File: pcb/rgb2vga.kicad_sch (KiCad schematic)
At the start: 43 parts, among them J1 GPIO_0, J2 RGB_IN, J3 COCO3_RGB_IN, J4 C_VIDEO_IN, J5 GPIO_1, J6 VGA_OUT, J7 Conn_01x03_Male, SW1 SW_DIP_x10, SW2 SW_DP3T, U1 LM1881

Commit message: fiducials, pics
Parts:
- added JP1: lowpass, 000_LOCAL:JP_0805, symbol 000_LOCAL:SolderJumper_2_Bridged
- R29: footprint 000_LOCAL:R_0805_SJC -> 000_LOCAL:R_0805
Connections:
- net RGB_CS: now also JP1.1 (A)
- net at C1.1, C4.1, R29.2: now also JP1.2 (B)
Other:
- note added: "optional 500kHz low pass cut JP1"
- note removed: "optional 500kHz low pass"
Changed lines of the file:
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@@
 	(title_block
 		(title "DE0-NANO RGB2VGA")
-		(date "2024-01-07")
-		(rev "008")
+		(date "2024-07-26")
+		(rev "009")
 		(company "Brian K. White - b.kenyon.w@gmail.com")
 		(comment 1 "Original Design by Luis Antoniosi 2014")
@@
 	)
 	(junction
+		(at 180.34 134.62)
+		(diameter 0)
+		(color 0 0 0 0)
+	)
+	(junction
 		(at 127 81.28)
 		(diameter 0)
@@
 	)
 	(junction
+		(at 172.72 127)
+		(diameter 0)
+		(color 0 0 0 0)
+	)
+	(junction
 		(at 69.85 38.1)
 		(diameter 0)
@@
 	(wire
 		(pts
-			(xy 172.72 134.62) (xy 187.96 134.62)
+			(xy 172.72 134.62) (xy 180.34 134.62)
 		)
 		(stroke
@@
 	(wire
 		(pts
+			(xy 180.34 134.62) (xy 187.96 134.62)
+		)
+		(stroke
+			(width 0)
+			(type default)
+		)
+	)
+	(wire
+		(pts
 			(xy 203.2 66.04) (xy 190.5 66.04)
 		)
@@
 	(wire
 		(pts
+			(xy 172.72 127) (xy 180.34 127)
+		)
+		(stroke
+			(width 0)
+			(type default)
+		)
+	)
+	(wire
+		(pts
 			(xy 44.45 157.48) (xy 44.45 165.1)
 		)
@@
 		)
 	)
-	(text "optional\n500kHz\nlow pass"
+	(text "optional\n500kHz\nlow pass\ncut JP1"
 		(exclude_from_sim no)
 		(at 167.64 124.46 0)
@@
 	)
 	(symbol
+		(lib_id "000_LOCAL:SolderJumper_2_Bridged")
+		(at 180.34 130.81 270)
+		(unit 1)
+		(exclude_from_sim no)
+		(in_bom yes)
+		(on_board yes)
+		(dnp no)
+		(property "Reference" "JP1"
+			(at 180.848 126.238 90)
+			(effects
+				(font
+					(size 1.27 1.27)
+				)
+				(justify left)
+			)
+		)
+		(property "Value" "lowpass"
+			(at 180.594 124.206 90)
+			(effects
+				(font
+					(size 1.27 1.27)
+				)
+			)
+		)
+		(property "Footprint" "000_LOCAL:JP_0805"
+			(at 180.34 130.81 0)
+			(effects
+				(font
+					(size 1.27 1.27)
+				)
+				(hide yes)
+			)
+		)
+		(property "Datasheet" "~"
+			(at 180.34 130.81 0)
+			(effects
+				(font
+					(size 1.27 1.27)
+				)
+				(hide yes)
+			)
+		)
+		(property "Description" "Solder Jumper, 2-pole, closed/bridged"
+			(at 180.34 130.81 0)
+			(effects
+				(font
+					(size 1.27 1.27)
+				)
+				(hide yes)
+			)
+		)
+		(pin "1"
+		)
+		(pin "2"
+		)
+		(instances
+			(project ""
+				(path "/dc38b7f3-94d8-459d-903b-54a6ae2cb037"
+					(reference "JP1")
+					(unit 1)
+				)
+			)
+		)
+	)
+	(symbol
 		(lib_id "000_LOCAL:GND")
 		(at 133.35 127 0)
@@
 			)
 		)
-		(property "Footprint" "000_LOCAL:R_0805_SJC"
+		(property "Footprint" "000_LOCAL:R_0805"
 			(at 172.72 130.81 0)
 			(effects

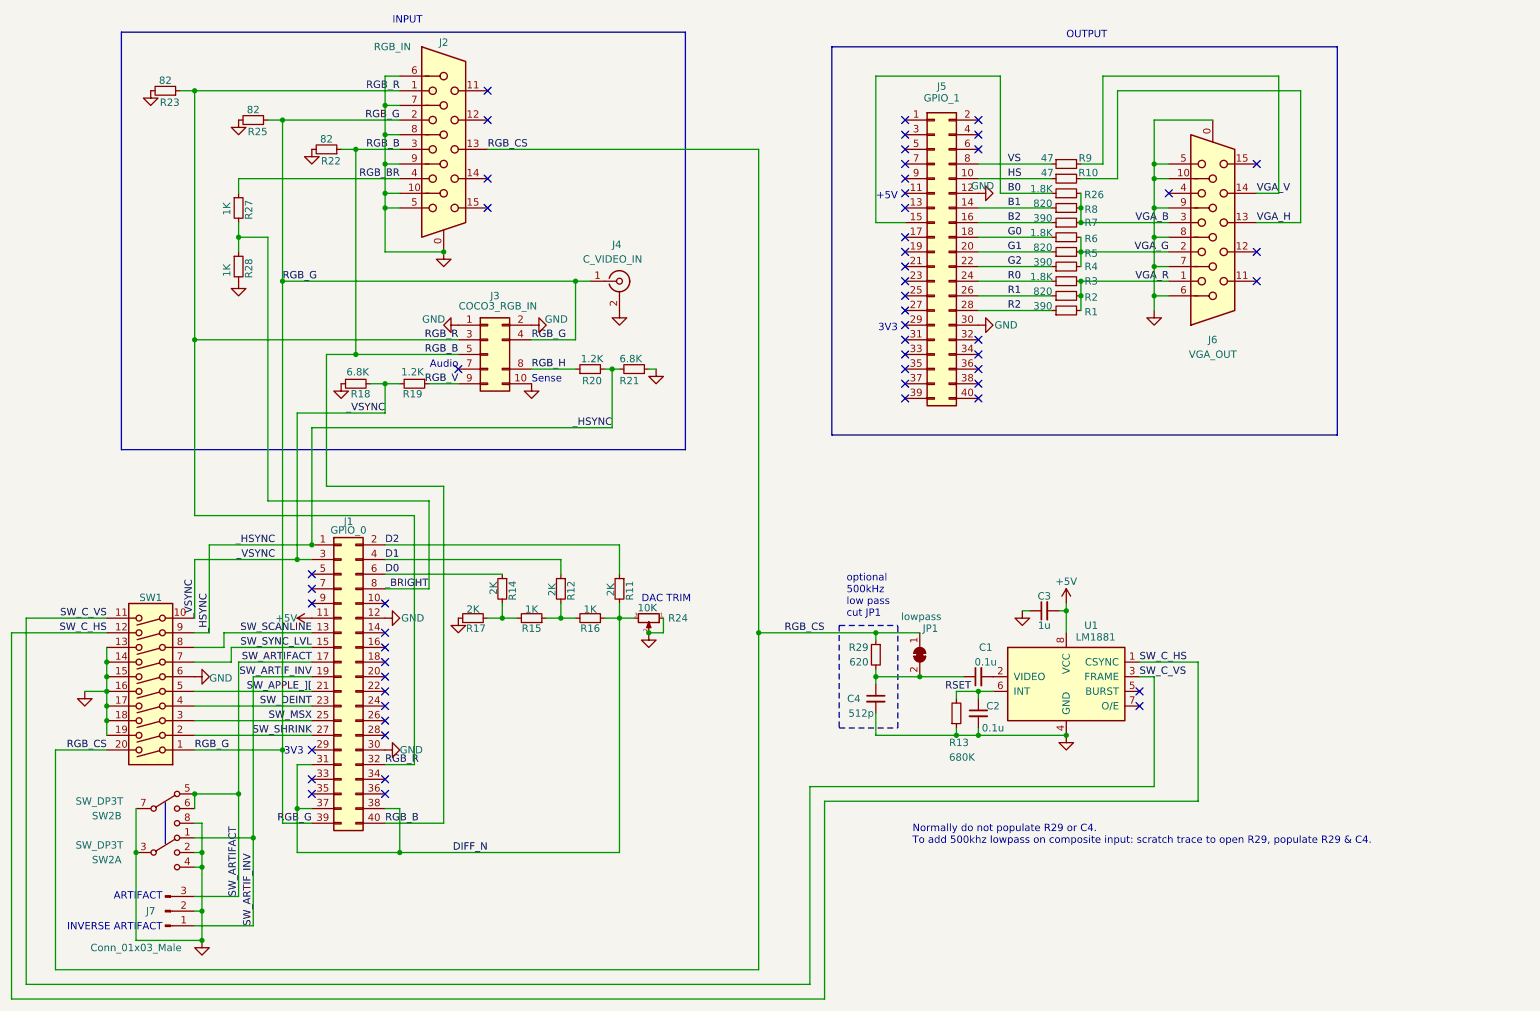
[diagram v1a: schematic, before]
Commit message: C4 510p, dnp fiducials, pnp export
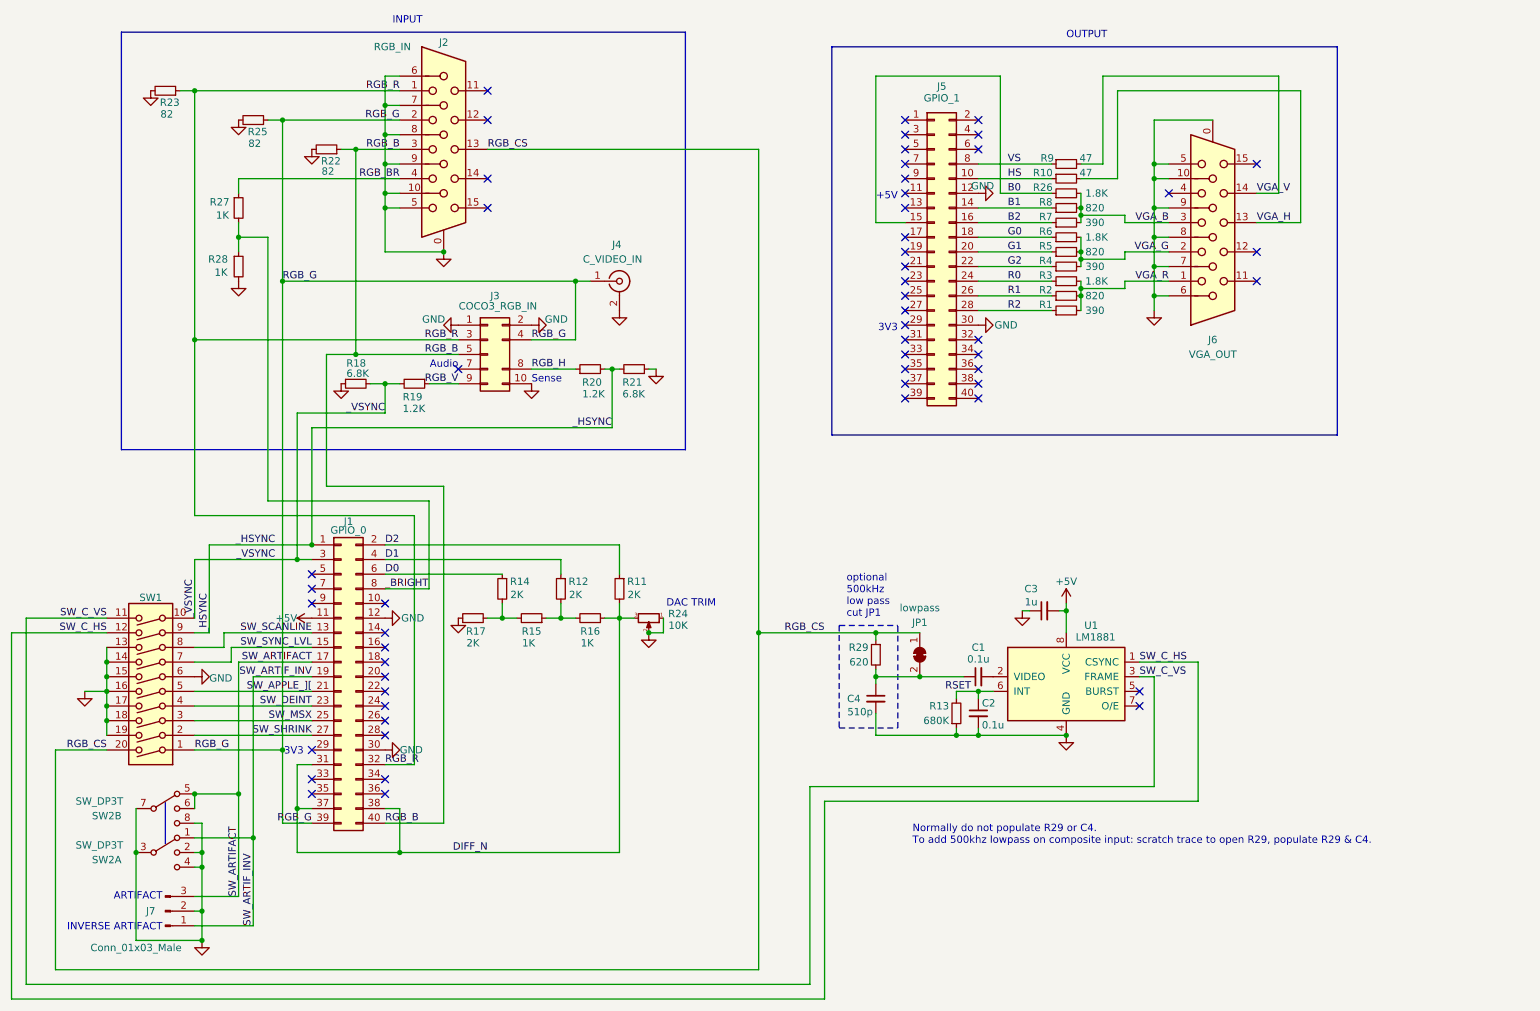
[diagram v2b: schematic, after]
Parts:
- C4: value 512p -> 510p

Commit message: export bom, centroid
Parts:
- C1, C2: MPN (none) -> KGM21NR71H104JT
- C3: MPN (none) -> CL21B105KAFNNNE
- C4: MPN (none) -> C0805C511F3HAC7800; now not fitted
- J1: value GPIO_0 -> PinSocket_02x20_P2.54mm_Vertical_tht; Label (none) -> GPIO_0; MPN (none) -> SFH11-PBPC-D20-ST-BK
- J2: value RGB_IN -> HD15F_horizontal_tht; Label (none) -> RGB_IN; MPN (none) -> HD15-SN-25
- J3: value COCO3_RGB_IN -> IDC-Header_2x05_P2.54mm_Horizontal_tht; Label (none) -> COCO3_RGB_IN; MPN (none) -> 302-R101
- J4: value C_VIDEO_IN -> RCA_horizontal_tht; Label (none) -> C_VIDEO_IN; MPN (none) -> RCJ-014
- J5: value GPIO_1 -> PinSocket_02x20_P2.54mm_Vertical_tht; Label (none) -> GPIO_1; MPN (none) -> SFH11-PBPC-D20-ST-BK
- J6: value VGA_OUT -> HD15F_horizontal_tht; Label (none) -> VGA_OUT; MPN (none) -> HD15-SN-25
- J7: MPN (none) -> PRPC003SBAN-M71RC
- JP1: now left out of the parts list
- R1, R4, R7: MPN (none) -> ERA-6AEB391V
- R10, R9: MPN (none) -> ERA-6AEB470V
- R11, R12, R14, R17: MPN (none) -> ERA-6AEB202V
- R13: MPN (none) -> ERA-6AEB684V
- R15, R16, R27, R28: MPN (none) -> ERA-6AEB102V
- R18, R21: MPN (none) -> ERA-6AEB682V
- R19, R20: MPN (none) -> ERA-6AEB122V
- R2, R5, R8: MPN (none) -> ERA-6AEB821V
- R22, R23, R25: MPN (none) -> ERA-6AEB820V
- R24: MPN (none) -> 3006P-1-103LF
- R26, R3, R6: MPN (none) -> ERA-6AEB182V
- R29: MPN (none) -> ERA-6AEB621V; now not fitted
- SW1: MPN (none) -> DS04-254-2-10BK-SMT
- SW2: MPN (none) -> CL-SB-23A-11T
- U1: MPN (none) -> LM1881MX/NOPB

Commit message: silkscreen & pics
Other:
- note added: "ADC TRIM"
- note removed: "DAC TRIM"
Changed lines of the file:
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@@
 	(title_block
 		(title "DE0-NANO RGB2VGA")
-		(date "2024-08-06")
-		(rev "010")
+		(date "2024-08-30")
+		(rev "018")
 		(company "Brian K. White - b.kenyon.w@gmail.com")
 		(comment 1 "Original Design by Luis Antoniosi 2014")
@@
 		)
 	)
-	(text "DAC TRIM"
+	(text "ADC TRIM"
 		(exclude_from_sim no)
 		(at 136.398 122.682 0)

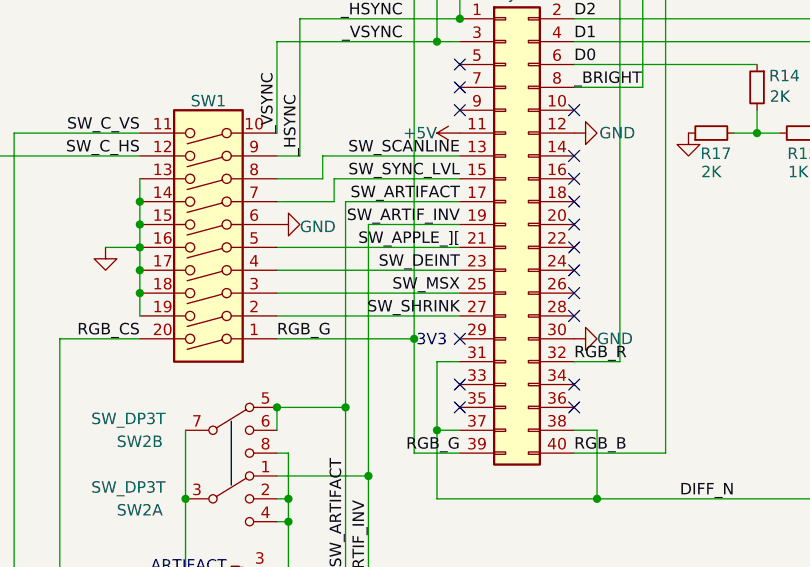
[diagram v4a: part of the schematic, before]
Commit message: rename msx switch to offset
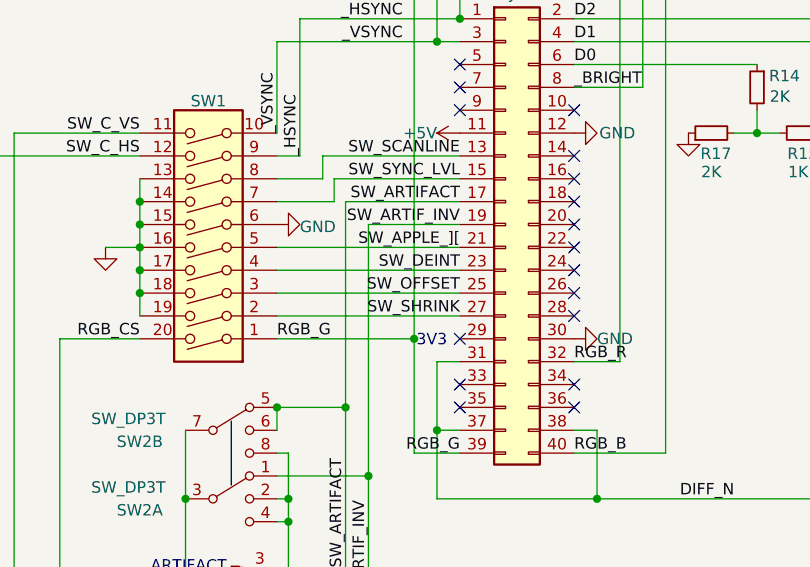
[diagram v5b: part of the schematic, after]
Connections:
- net SW_MSX renamed SW_OFFSET
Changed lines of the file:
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@@
 		)
 	)
-	(label "SW_MSX"
+	(label "SW_OFFSET"
 		(at 74.93 142.24 180)
 		(fields_autoplaced yes)
